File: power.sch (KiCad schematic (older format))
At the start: 12 parts, among them P301 USB_A, U301 MCP1623/24, U302 MCP1700T

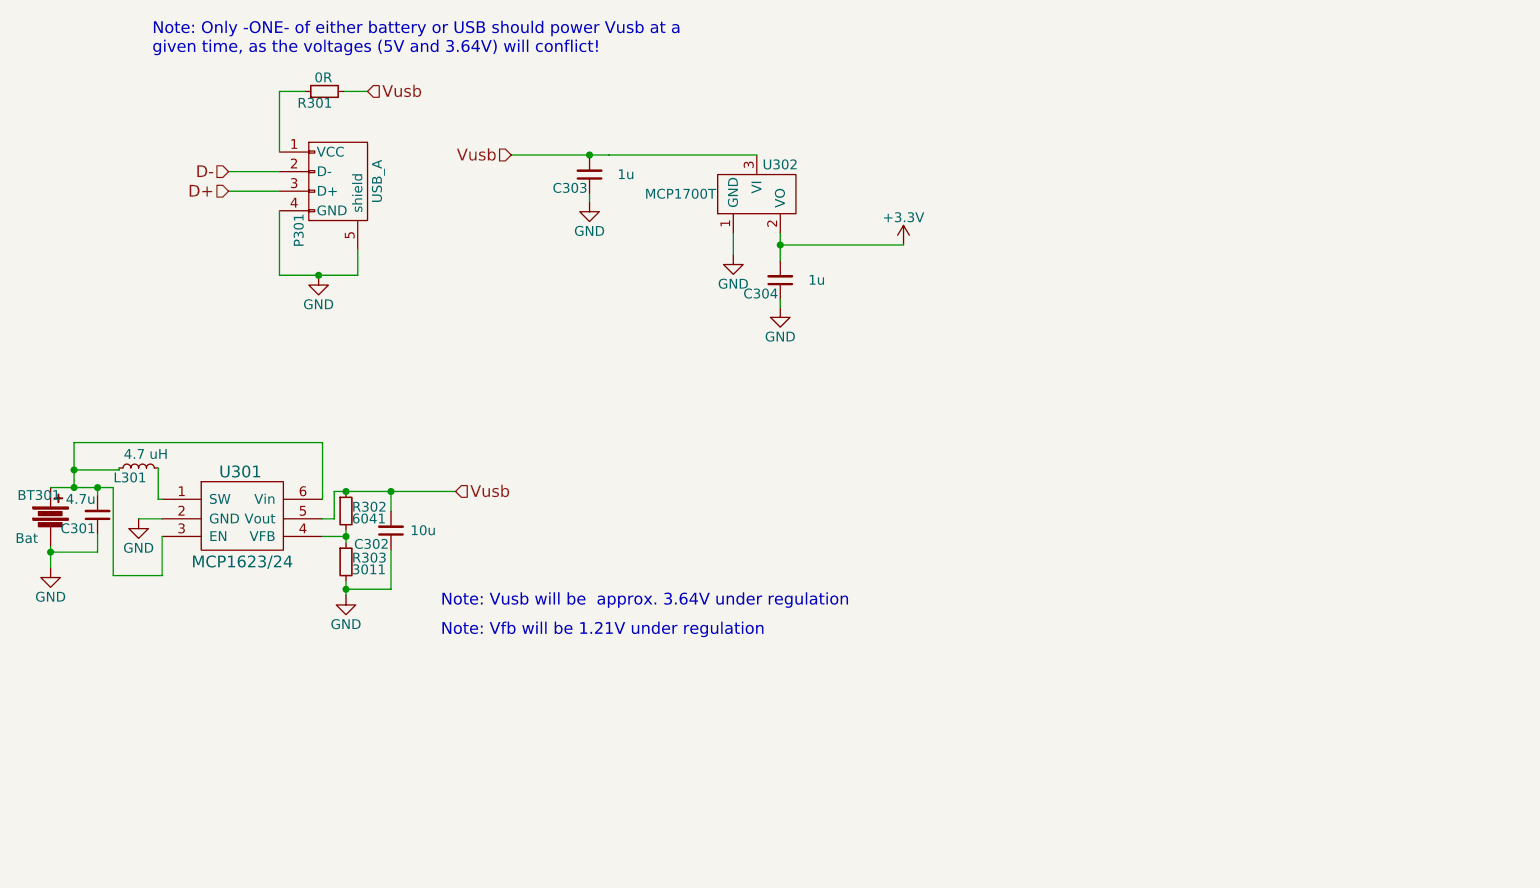
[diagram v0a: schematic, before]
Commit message: cleaned up schematic, updated ir receive/transmit
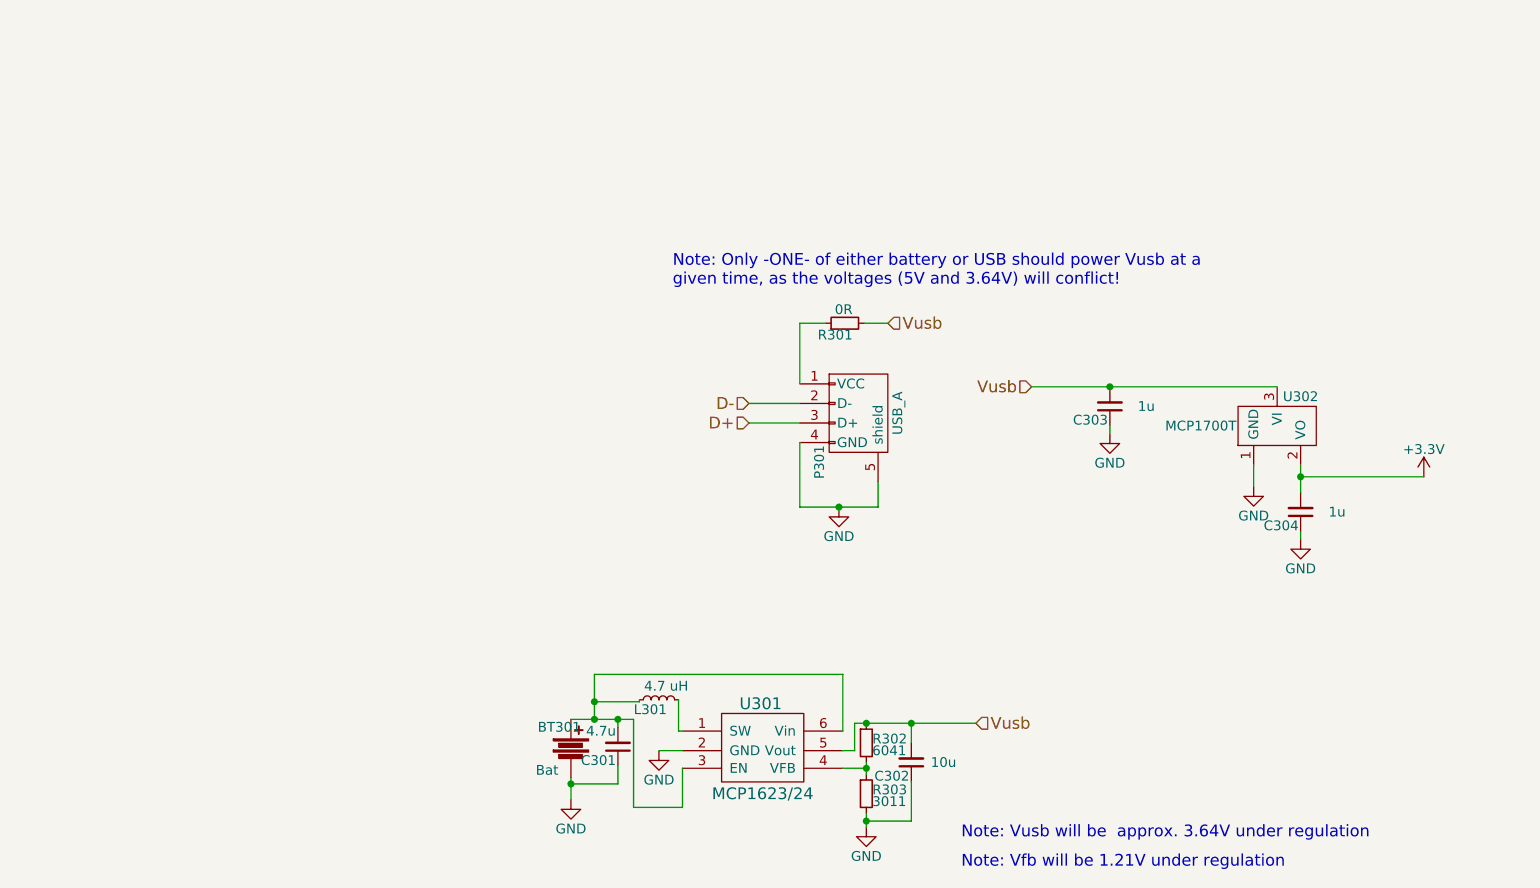
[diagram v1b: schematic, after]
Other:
- moved on the sheet: BT301, C301, C302, C303, C304, L301, P301, R301, R302, R303, U301, U302
